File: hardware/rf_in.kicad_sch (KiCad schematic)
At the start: 12 parts

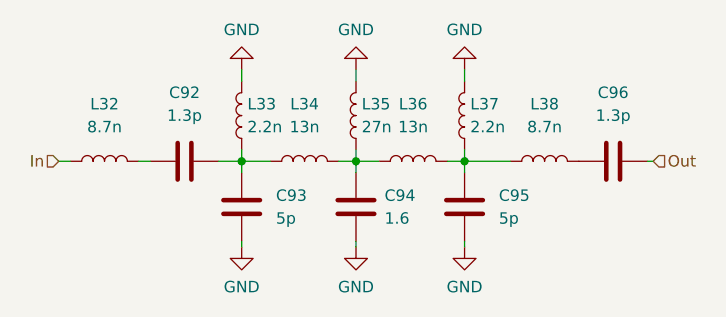
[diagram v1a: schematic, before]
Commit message: Update FEM hardware design for production version
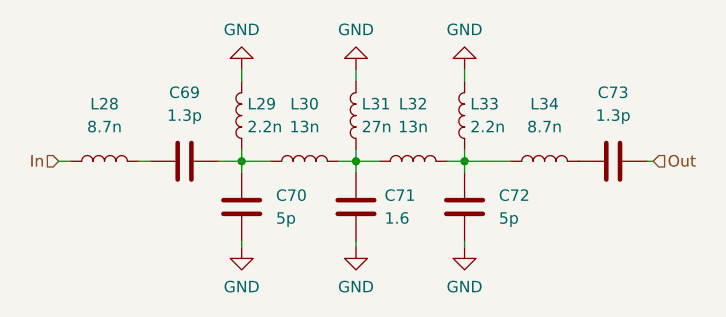
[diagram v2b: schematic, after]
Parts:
- renumbered C92 to C69, C93 to C70, C94 to C71, C95 to C72, C96 to C73, L32 to L28, L33 to L29, L34 to L30, L35 to L31, L36 to L32, L37 to L33, L38 to L34
